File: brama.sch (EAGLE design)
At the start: 50 parts, among them IC1 AT90USB162A, J1 AVR_SPI_PRG_6OFFSET_PADS

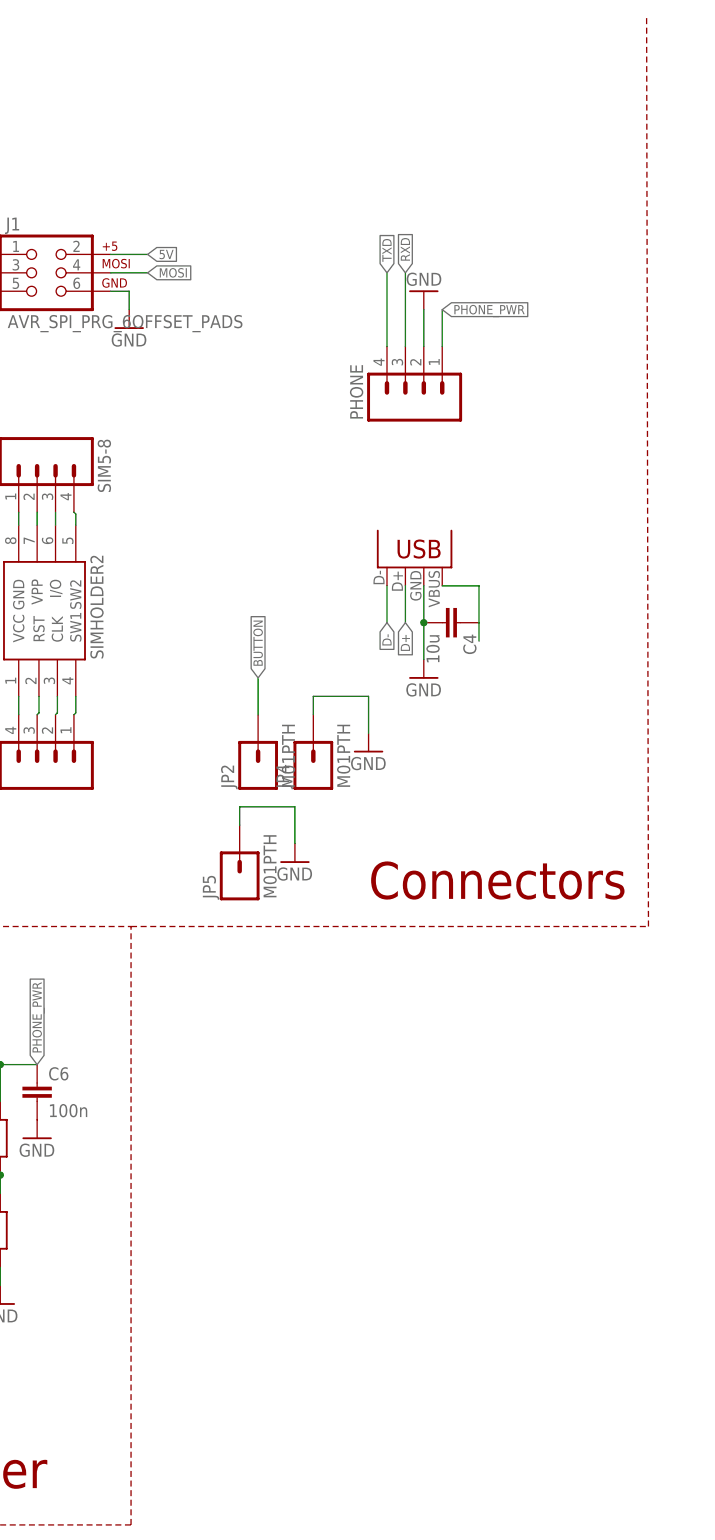
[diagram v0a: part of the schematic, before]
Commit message: DC-DC converter
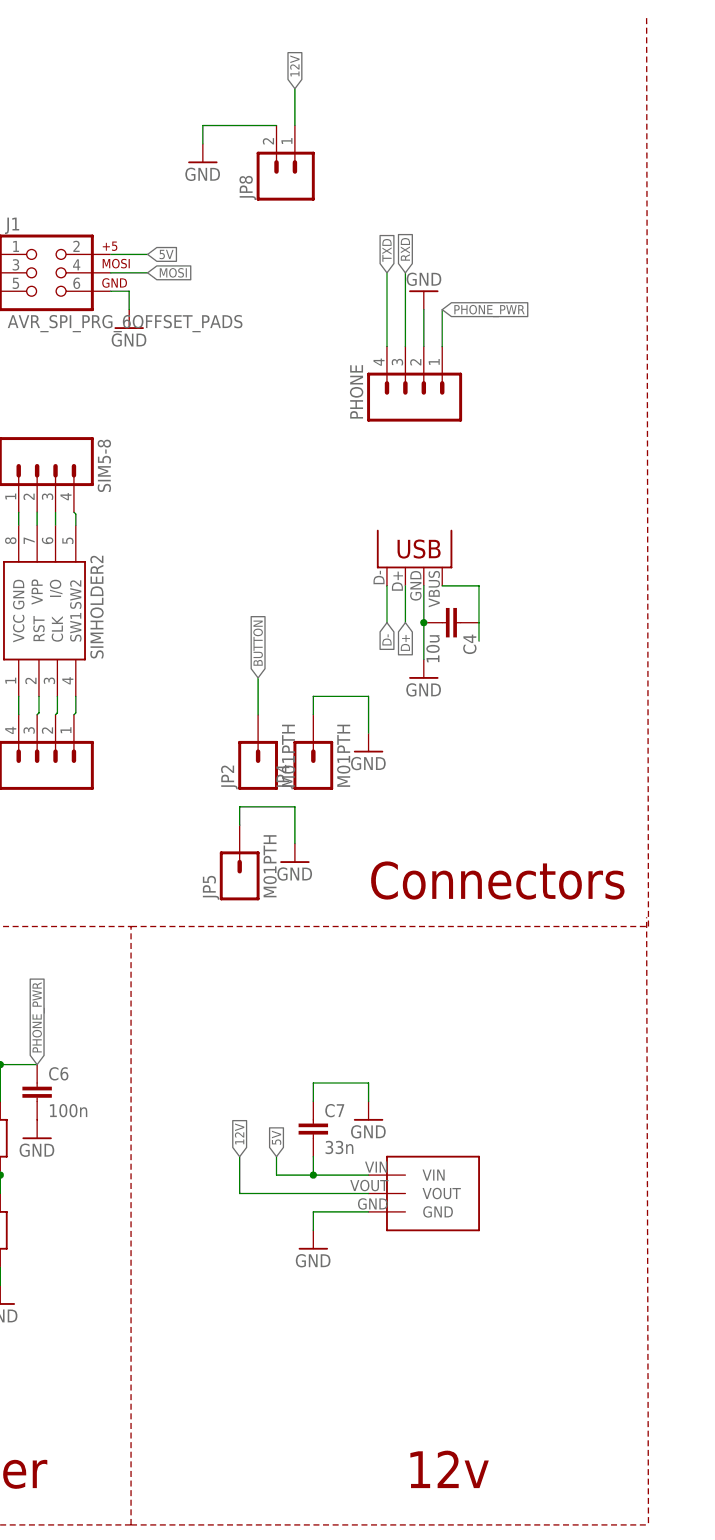
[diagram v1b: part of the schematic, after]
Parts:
- added C7: 33n, rcl:C-EUC0805
- added JP8: (no value), SparkFun-Connectors:M02PTH3
- added U$6: U3V12F12, pololu DC-DC converters:U3V12F12
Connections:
- new net 12V: JP8.1, U$6.VOUT
- net 5V: now also C7.2, U$6.VIN
- net GND: now also C7.1, JP8.2, U$6.GND
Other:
- note added: "12v"
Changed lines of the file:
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@@
 <part name="JP6" library="SparkFun-Connectors" deviceset="M01" device="PTH"/>
 <part name="JP7" library="SparkFun-Connectors" deviceset="M01" device="PTH"/>
+<part name="U$6" library="pololu DC-DC converters" deviceset="U3V12F12" device=""/>
+<part name="C7" library="rcl" deviceset="C-EU" device="C0805" value="33n"/>
+<part name="GND18" library="SparkFun-Aesthetics" deviceset="GND" device=""/>
+<part name="GND19" library="SparkFun-Aesthetics" deviceset="GND" device=""/>
+<part name="JP8" library="SparkFun-Connectors" deviceset="M02" device="PTH3"/>
+<part name="GND20" library="SparkFun-Aesthetics" deviceset="GND" device=""/>
 </parts>
 <sheets>
@@
 <text x="119.38" y="53.34" size="5.08" layer="94">LEDs</text>
 <text x="160.02" y="53.34" size="5.08" layer="94">Power</text>
+<text x="228.6" y="53.34" size="5.08" layer="94">12v</text>
+<wire x1="190.754" y1="48.26" x2="261.874" y2="48.26" width="0.1524" layer="94" style="shortdash"/>
+<wire x1="262.128" y1="48.514" x2="261.874" y2="132.08" width="0.1524" layer="94" style="shortdash"/>
 </plain>
 <instances>
@@
 <instance part="JP6" gate="G$1" x="104.14" y="86.36" rot="R90"/>
 <instance part="JP7" gate="G$1" x="78.74" y="86.36" rot="R90"/>
+<instance part="U$6" gate="G$1" x="226.06" y="88.9"/>
+<instance part="C7" gate="G$1" x="215.9" y="104.14"/>
+<instance part="GND18" gate="1" x="215.9" y="86.36"/>
+<instance part="GND19" gate="1" x="223.52" y="104.14"/>
+<instance part="JP8" gate="G$1" x="213.36" y="233.68" rot="R90"/>
+<instance part="GND20" gate="1" x="200.66" y="236.22"/>
 </instances>
 <busses>
@@
 <pinref part="GND17" gate="1" pin="GND"/>
 </segment>
+<segment>
+<pinref part="U$6" gate="G$1" pin="GND"/>
+<pinref part="GND18" gate="1" pin="GND"/>
+<wire x1="223.52" y1="91.44" x2="215.9" y2="91.44" width="0.1524" layer="91"/>
+<wire x1="215.9" y1="91.44" x2="215.9" y2="88.9" width="0.1524" layer="91"/>
+</segment>
+<segment>
+<pinref part="C7" gate="G$1" pin="1"/>
+<wire x1="215.9" y1="106.68" x2="215.9" y2="109.22" width="0.1524" layer="91"/>
+<wire x1="215.9" y1="109.22" x2="223.52" y2="109.22" width="0.1524" layer="91"/>
+<wire x1="223.52" y1="109.22" x2="223.52" y2="106.68" width="0.1524" layer="91"/>
+<pinref part="GND19" gate="1" pin="GND"/>
+</segment>
+<segment>
+<pinref part="JP8" gate="G$1" pin="2"/>
+<wire x1="210.82" y1="241.3" x2="200.66" y2="241.3" width="0.1524" layer="91"/>
+<wire x1="200.66" y1="241.3" x2="200.66" y2="238.76" width="0.1524" layer="91"/>
+<pinref part="GND20" gate="1" pin="GND"/>
+</segment>
 </net>
 <net name="5V" class="0">
@@
 <pinref part="C4" gate="G$1" pin="1"/>
 <wire x1="238.76" y1="172.72" x2="238.76" y2="170.18" width="0.1524" layer="91"/>
+</segment>
+<segment>
+<pinref part="U$6" gate="G$1" pin="VIN"/>
+<wire x1="223.52" y1="96.52" x2="215.9" y2="96.52" width="0.1524" layer="91"/>
+<pinref part="C7" gate="G$1" pin="2"/>
+<wire x1="215.9" y1="96.52" x2="210.82" y2="96.52" width="0.1524" layer="91"/>
+<wire x1="215.9" y1="99.06" x2="215.9" y2="96.52" width="0.1524" layer="91"/>
+<junction x="215.9" y="96.52"/>
+<wire x1="210.82" y1="96.52" x2="210.82" y2="99.06" width="0.1524" layer="91"/>
+<label x="210.82" y="99.06" size="1.27" layer="95" rot="R90" xref="yes"/>
 </segment>
 </net>
@@
 </segment>
 </net>
+<net name="12V" class="0">
+<segment>
+<pinref part="U$6" gate="G$1" pin="VOUT"/>
+<wire x1="223.52" y1="93.98" x2="205.74" y2="93.98" width="0.1524" layer="91"/>
+<wire x1="205.74" y1="93.98" x2="205.74" y2="99.06" width="0.1524" layer="91"/>
+<label x="205.74" y="99.06" size="1.27" layer="95" rot="R90" xref="yes"/>
+</segment>
+<segment>
+<pinref part="JP8" gate="G$1" pin="1"/>
+<wire x1="213.36" y1="241.3" x2="213.36" y2="246.38" width="0.1524" layer="91"/>
+<label x="213.36" y="246.38" size="1.27" layer="95" rot="R90" xref="yes"/>
+</segment>
+</net>

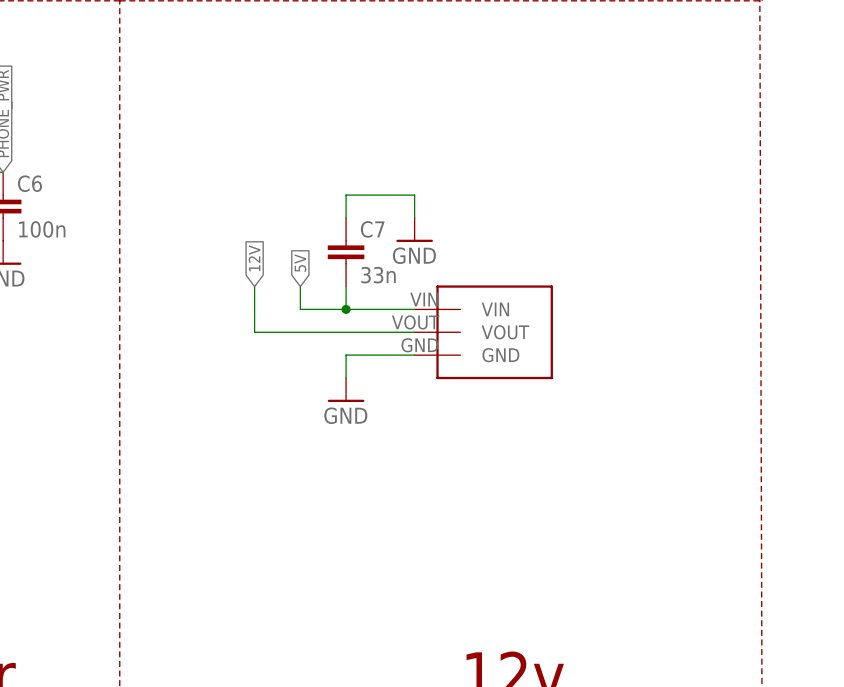
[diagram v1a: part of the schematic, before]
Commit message: LM2704 Step-Up DC/DC Converter
http://www.ti.com.cn/general/cn/docs/lit/getliterature.tsp?genericPartNumber=lm2704&fileType=pdf
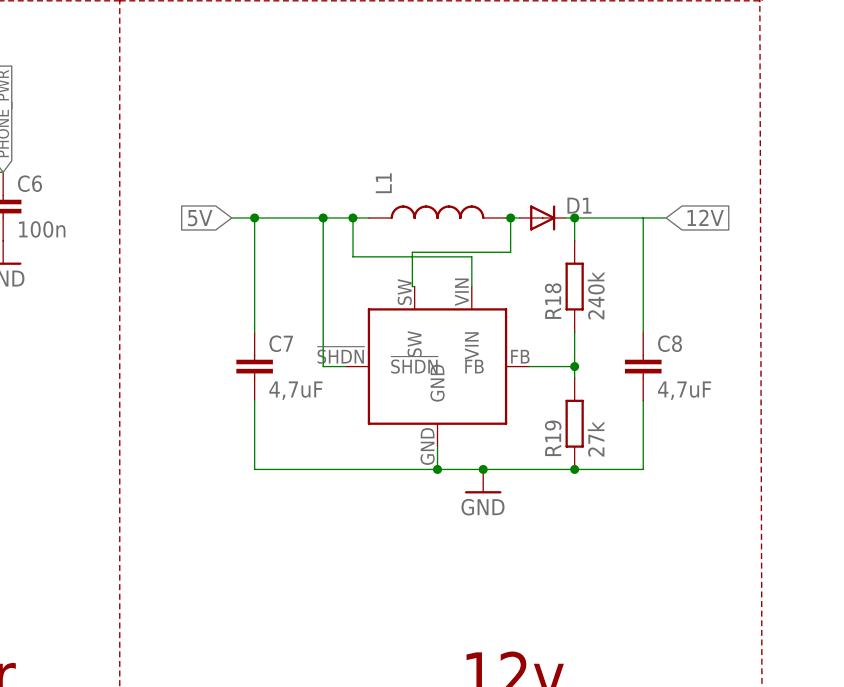
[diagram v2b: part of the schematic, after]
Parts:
- added C8: 4,7uF, rcl:C-EUC0805
- added D1: (no value), SparkFun-DiscreteSemi:DIODESMB
- added L1: (no value), SparkFun-Passives:INDUCTOR0805
- added R18: 240k, rcl:R-EU_R0805
- added R19: 27k, rcl:R-EU_R0805
- C7: value 33n -> 4,7uF
- U$6: value U3V12F12 -> LM2704MF-ADJ; device pololu DC-DC converters:U3V12F12 -> Step-Up:LM2704MF-ADJ
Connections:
- new net N$31: D1.A, L1.2, U$6.SW
- new net N$34: R18.1, R19.2, U$6.FB
- net 12V: now also C8.1, D1.C, R18.2; no longer U$6.VOUT
- net 5V: now also C7.1, L1.1, U$6.!SHDN; no longer C7.2
- net GND: now also C7.2, C8.2, R19.1; no longer C7.1
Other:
- moved on the sheet: C7
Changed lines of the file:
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@@
 <part name="JP6" library="SparkFun-Connectors" deviceset="M01" device="PTH"/>
 <part name="JP7" library="SparkFun-Connectors" deviceset="M01" device="PTH"/>
-<part name="U$6" library="pololu DC-DC converters" deviceset="U3V12F12" device=""/>
-<part name="C7" library="rcl" deviceset="C-EU" device="C0805" value="33n"/>
-<part name="GND18" library="SparkFun-Aesthetics" deviceset="GND" device=""/>
-<part name="GND19" library="SparkFun-Aesthetics" deviceset="GND" device=""/>
 <part name="JP8" library="SparkFun-Connectors" deviceset="M02" device="PTH3"/>
 <part name="GND20" library="SparkFun-Aesthetics" deviceset="GND" device=""/>
+<part name="U$6" library="Step-Up" deviceset="LM2704MF-ADJ" device=""/>
+<part name="L1" library="SparkFun-Passives" deviceset="INDUCTOR" device="0805"/>
+<part name="C7" library="rcl" deviceset="C-EU" device="C0805" value="4,7uF"/>
+<part name="C8" library="rcl" deviceset="C-EU" device="C0805" value="4,7uF"/>
+<part name="R18" library="rcl" deviceset="R-EU_" device="R0805" value="240k"/>
+<part name="R19" library="rcl" deviceset="R-EU_" device="R0805" value="27k"/>
+<part name="D1" library="SparkFun-DiscreteSemi" deviceset="DIODE" device="SMB"/>
+<part name="GND18" library="SparkFun-Aesthetics" deviceset="GND" device=""/>
 </parts>
 <sheets>
@@
 <instance part="JP6" gate="G$1" x="104.14" y="86.36" rot="R90"/>
 <instance part="JP7" gate="G$1" x="78.74" y="86.36" rot="R90"/>
-<instance part="U$6" gate="G$1" x="226.06" y="88.9"/>
-<instance part="C7" gate="G$1" x="215.9" y="104.14"/>
-<instance part="GND18" gate="1" x="215.9" y="86.36"/>
-<instance part="GND19" gate="1" x="223.52" y="104.14"/>
 <instance part="JP8" gate="G$1" x="213.36" y="233.68" rot="R90"/>
 <instance part="GND20" gate="1" x="200.66" y="236.22"/>
+<instance part="U$6" gate="G$1" x="218.44" y="83.82"/>
+<instance part="L1" gate="G$1" x="226.06" y="106.68" rot="R90"/>
+<instance part="C7" gate="G$1" x="205.74" y="91.44"/>
+<instance part="C8" gate="G$1" x="248.92" y="91.44"/>
+<instance part="R18" gate="G$1" x="241.3" y="99.06" rot="R90"/>
+<instance part="R19" gate="G$1" x="241.3" y="83.82" rot="R90"/>
+<instance part="D1" gate="G$1" x="237.744" y="106.68"/>
+<instance part="GND18" gate="1" x="231.14" y="76.2"/>
 </instances>
 <busses>
@@
 </segment>
 <segment>
-<pinref part="U$6" gate="G$1" pin="GND"/>
-<pinref part="GND18" gate="1" pin="GND"/>
-<wire x1="223.52" y1="91.44" x2="215.9" y2="91.44" width="0.1524" layer="91"/>
-<wire x1="215.9" y1="91.44" x2="215.9" y2="88.9" width="0.1524" layer="91"/>
-</segment>
-<segment>
-<pinref part="C7" gate="G$1" pin="1"/>
-<wire x1="215.9" y1="106.68" x2="215.9" y2="109.22" width="0.1524" layer="91"/>
-<wire x1="215.9" y1="109.22" x2="223.52" y2="109.22" width="0.1524" layer="91"/>
-<wire x1="223.52" y1="109.22" x2="223.52" y2="106.68" width="0.1524" layer="91"/>
-<pinref part="GND19" gate="1" pin="GND"/>
-</segment>
-<segment>
 <pinref part="JP8" gate="G$1" pin="2"/>
 <wire x1="210.82" y1="241.3" x2="200.66" y2="241.3" width="0.1524" layer="91"/>
 <wire x1="200.66" y1="241.3" x2="200.66" y2="238.76" width="0.1524" layer="91"/>
 <pinref part="GND20" gate="1" pin="GND"/>
+</segment>
+<segment>
+<pinref part="C7" gate="G$1" pin="2"/>
+<wire x1="205.74" y1="78.74" x2="205.74" y2="86.36" width="0.1524" layer="91"/>
+<pinref part="C8" gate="G$1" pin="2"/>
+<wire x1="248.92" y1="78.74" x2="248.92" y2="86.36" width="0.1524" layer="91"/>
+<wire x1="205.74" y1="78.74" x2="226.06" y2="78.74" width="0.1524" layer="91"/>
+<pinref part="U$6" gate="G$1" pin="GND"/>
+<wire x1="226.06" y1="78.74" x2="231.14" y2="78.74" width="0.1524" layer="91"/>
+<wire x1="231.14" y1="78.74" x2="241.3" y2="78.74" width="0.1524" layer="91"/>
+<wire x1="241.3" y1="78.74" x2="248.92" y2="78.74" width="0.1524" layer="91"/>
+<wire x1="226.06" y1="81.28" x2="226.06" y2="78.74" width="0.1524" layer="91"/>
+<junction x="226.06" y="78.74"/>
+<pinref part="R19" gate="G$1" pin="1"/>
+<junction x="241.3" y="78.74"/>
+<pinref part="GND18" gate="1" pin="GND"/>
+<junction x="231.14" y="78.74"/>
 </segment>
 </net>
@@
 </segment>
 <segment>
+<pinref part="L1" gate="G$1" pin="1"/>
+<wire x1="218.44" y1="106.68" x2="216.662" y2="106.68" width="0.1524" layer="91"/>
+<pinref part="U$6" gate="G$1" pin="!SHDN"/>
+<wire x1="216.662" y1="106.68" x2="213.36" y2="106.68" width="0.1524" layer="91"/>
+<wire x1="215.9" y1="90.17" x2="213.36" y2="90.17" width="0.1524" layer="91"/>
+<wire x1="213.36" y1="90.17" x2="213.36" y2="106.68" width="0.1524" layer="91"/>
+<junction x="213.36" y="106.68"/>
+<wire x1="213.36" y1="106.68" x2="205.74" y2="106.68" width="0.1524" layer="91"/>
+<pinref part="C7" gate="G$1" pin="1"/>
+<wire x1="205.74" y1="106.68" x2="203.2" y2="106.68" width="0.1524" layer="91"/>
+<wire x1="205.74" y1="106.68" x2="205.74" y2="93.98" width="0.1524" layer="91"/>
+<junction x="205.74" y="106.68"/>
+<label x="203.2" y="106.68" size="1.778" layer="95" rot="R180" xref="yes"/>
 <pinref part="U$6" gate="G$1" pin="VIN"/>
-<wire x1="223.52" y1="96.52" x2="215.9" y2="96.52" width="0.1524" layer="91"/>
-<pinref part="C7" gate="G$1" pin="2"/>
-<wire x1="215.9" y1="96.52" x2="210.82" y2="96.52" width="0.1524" layer="91"/>
-<wire x1="215.9" y1="99.06" x2="215.9" y2="96.52" width="0.1524" layer="91"/>
-<junction x="215.9" y="96.52"/>
-<wire x1="210.82" y1="96.52" x2="210.82" y2="99.06" width="0.1524" layer="91"/>
-<label x="210.82" y="99.06" size="1.27" layer="95" rot="R90" xref="yes"/>
+<wire x1="229.87" y1="99.06" x2="229.87" y2="102.362" width="0.1524" layer="91"/>
+<wire x1="229.87" y1="102.362" x2="216.662" y2="102.362" width="0.1524" layer="91"/>
+<wire x1="216.662" y1="102.362" x2="216.662" y2="106.68" width="0.1524" layer="91"/>
+<junction x="216.662" y="106.68"/>
 </segment>
 </net>
@@
 <net name="12V" class="0">
 <segment>
-<pinref part="U$6" gate="G$1" pin="VOUT"/>
-<wire x1="223.52" y1="93.98" x2="205.74" y2="93.98" width="0.1524" layer="91"/>
-<wire x1="205.74" y1="93.98" x2="205.74" y2="99.06" width="0.1524" layer="91"/>
-<label x="205.74" y="99.06" size="1.27" layer="95" rot="R90" xref="yes"/>
-</segment>
-<segment>
 <pinref part="JP8" gate="G$1" pin="1"/>
 <wire x1="213.36" y1="241.3" x2="213.36" y2="246.38" width="0.1524" layer="91"/>
 <label x="213.36" y="246.38" size="1.27" layer="95" rot="R90" xref="yes"/>
 </segment>
-</net>
+<segment>
+<pinref part="D1" gate="G$1" pin="C"/>
+<pinref part="R18" gate="G$1" pin="2"/>
+<wire x1="240.284" y1="106.68" x2="241.3" y2="106.68" width="0.1524" layer="91"/>
+<wire x1="241.3" y1="106.68" x2="241.3" y2="104.14" width="0.1524" layer="91"/>
+<pinref part="C8" gate="G$1" pin="1"/>
+<wire x1="241.3" y1="106.68" x2="248.92" y2="106.68" width="0.1524" layer="91"/>
+<wire x1="248.92" y1="106.68" x2="248.92" y2="93.98" width="0.1524" layer="91"/>
+<junction x="241.3" y="106.68"/>
+<wire x1="248.92" y1="106.68" x2="251.46" y2="106.68" width="0.1524" layer="91"/>
+<label x="251.46" y="106.68" size="1.778" layer="95" xref="yes"/>
+</segment>
+</net>
+<net name="N$34" class="0">
+<segment>
+<pinref part="R19" gate="G$1" pin="2"/>
+<pinref part="R18" gate="G$1" pin="1"/>
+<wire x1="241.3" y1="88.9" x2="241.3" y2="90.17" width="0.1524" layer="91"/>
+<pinref part="U$6" gate="G$1" pin="FB"/>
+<wire x1="241.3" y1="90.17" x2="241.3" y2="93.98" width="0.1524" layer="91"/>
+<wire x1="236.22" y1="90.17" x2="241.3" y2="90.17" width="0.1524" layer="91"/>
+<junction x="241.3" y="90.17"/>
+</segment>
+</net>
+<net name="N$31" class="0">
+<segment>
+<pinref part="L1" gate="G$1" pin="2"/>
+<wire x1="233.68" y1="106.68" x2="234.188" y2="106.68" width="0.1524" layer="91"/>
+<pinref part="D1" gate="G$1" pin="A"/>
+<pinref part="U$6" gate="G$1" pin="SW"/>
+<wire x1="234.188" y1="106.68" x2="235.204" y2="106.68" width="0.1524" layer="91"/>
+<wire x1="223.52" y1="99.06" x2="223.266" y2="99.06" width="0.1524" layer="91"/>
+<wire x1="223.266" y1="99.06" x2="223.266" y2="102.87" width="0.1524" layer="91"/>
+<wire x1="223.266" y1="102.87" x2="234.188" y2="102.87" width="0.1524" layer="91"/>
+<wire x1="234.188" y1="102.87" x2="234.188" y2="106.68" width="0.1524" layer="91"/>
+<junction x="234.188" y="106.68"/>
+</segment>
+</net>
